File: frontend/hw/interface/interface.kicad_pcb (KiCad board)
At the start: 2 copper layers, 60.2 x 34.5 mm, 11 parts, among them J1 Conn_01x05, J2 Conn_01x05, J3 Conn_01x06, J4 Conn_01x13, J5 Conn_02x13_Odd_Even

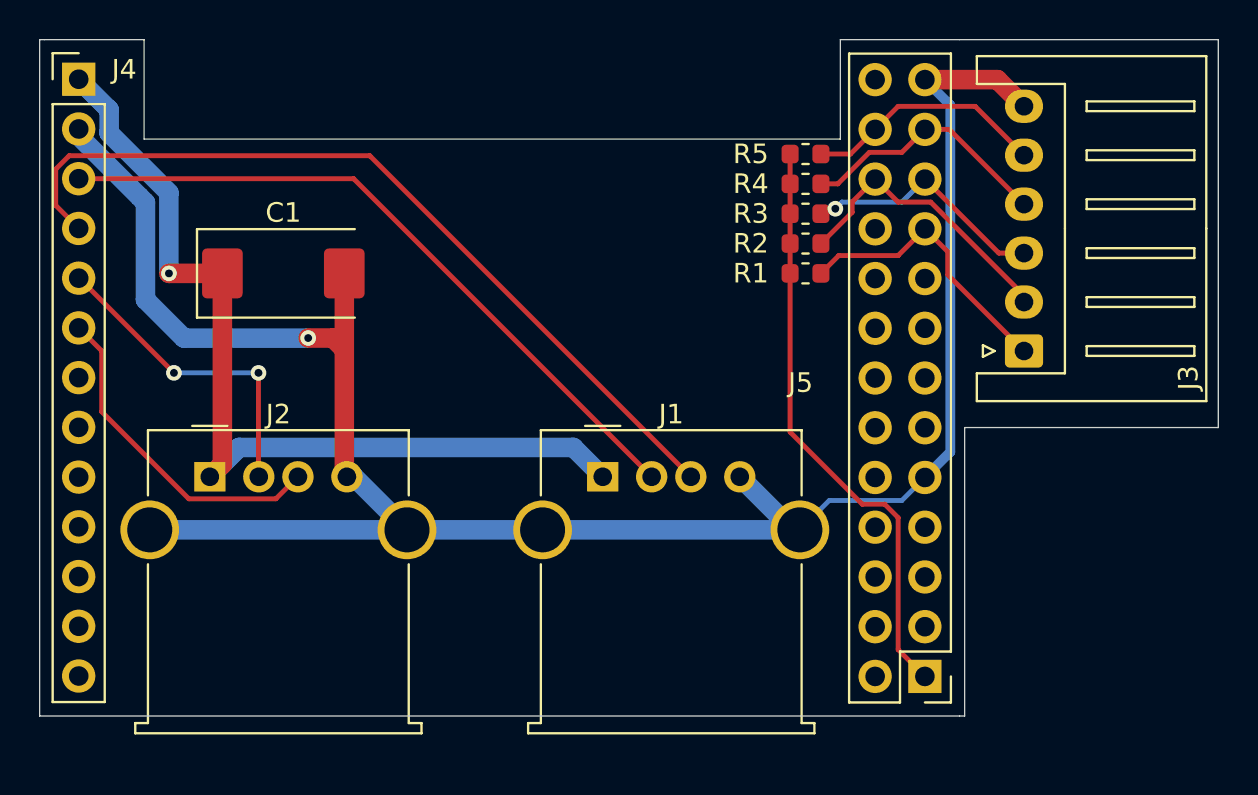
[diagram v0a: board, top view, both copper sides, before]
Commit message: Fix 3D view.
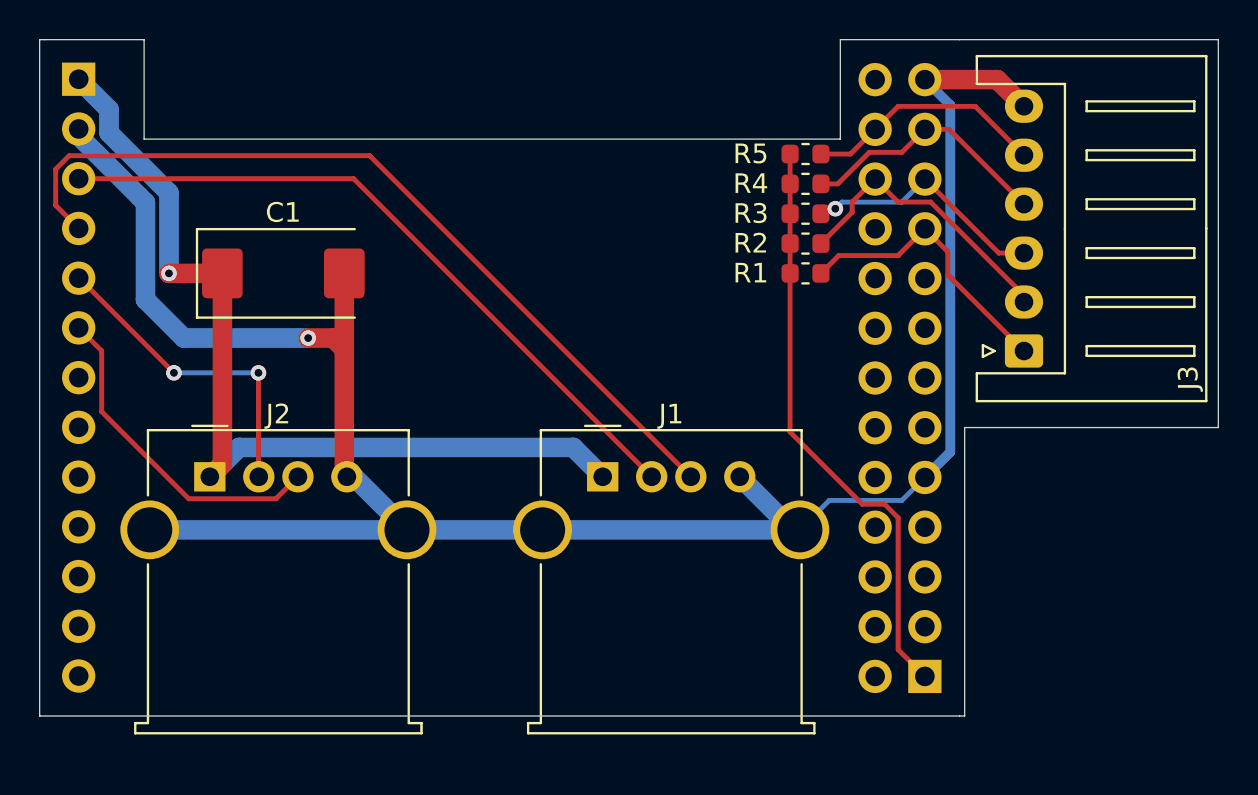
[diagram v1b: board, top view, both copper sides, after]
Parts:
- J4: footprint Connector_PinHeader_2.54mm:PinHeader_1x13_P2.54mm_Vertical -> Connector_PinSocket_2.54mm:PinSocket_1x13_P2.54mm_Vertical; moved to B.Cu
- J5: footprint Connector_PinHeader_2.54mm:PinHeader_2x13_P2.54mm_Vertical -> Connector_PinSocket_2.54mm:PinSocket_2x13_P2.54mm_Vertical; moved to B.Cu
- turned J4 to 180 degrees
- turned J5 to 0 degrees

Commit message: Adjust outline.
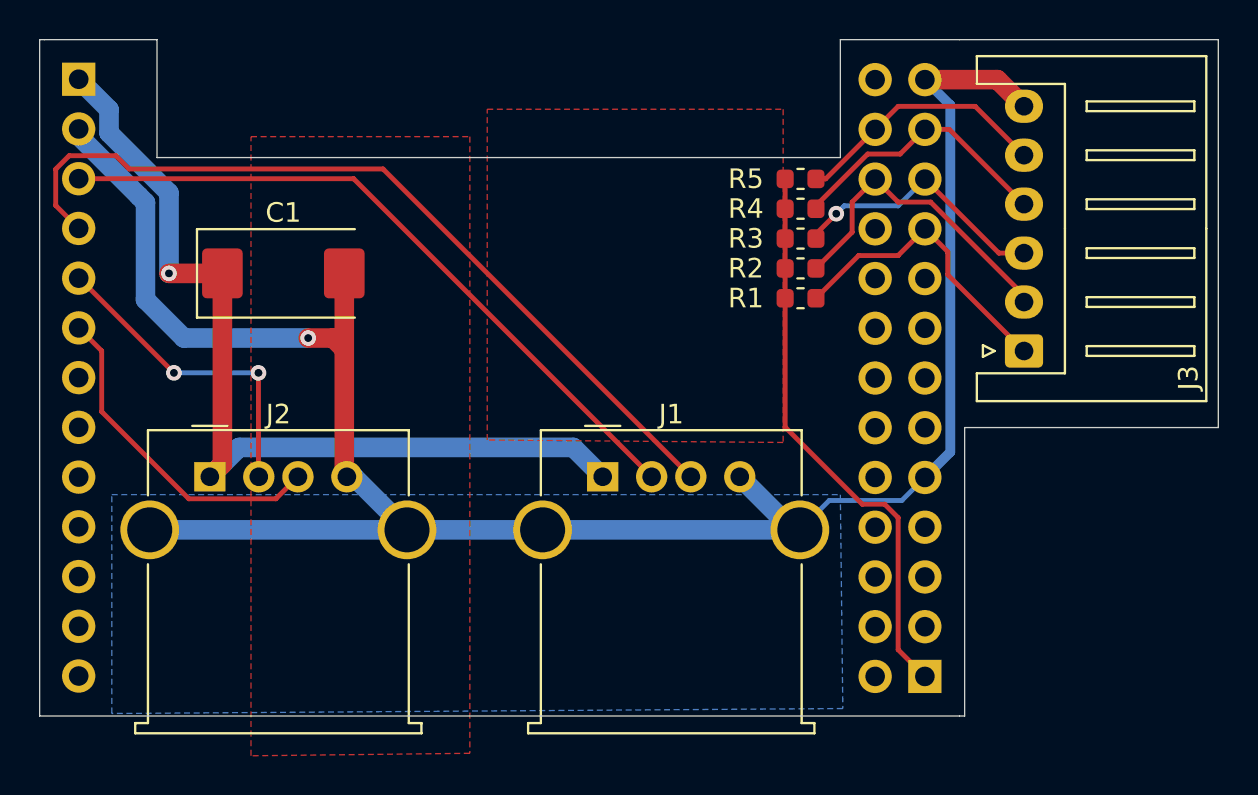
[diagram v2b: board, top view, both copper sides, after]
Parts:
- moved R1 1.30 mm to (86.9, 91.2)
- moved R2 1.30 mm to (86.9, 89.7)
- moved R3 1.30 mm to (86.9, 88.1)
- moved R4 1.30 mm to (86.9, 86.6)
- moved R5 1.30 mm to (86.9, 85.1)
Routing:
- net B2: track 14.8 -> 16.2 mm
- net +3V3: track 30.2 -> 29.0 mm
- net B3: track 12.7 -> 13.6 mm
- net B4: track 13.1 -> 14.0 mm
- net B1: track 14.6 -> 15.4 mm
- net B5: track 12.4 -> 13.2 mm
- added copper zone on F.Cu, net +3V3
- added copper zone on B.Cu, net GND
- added copper zone on F.Cu, net GND
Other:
- outline, holes or cut-outs redrawn
